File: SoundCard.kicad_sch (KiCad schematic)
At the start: 11 parts, among them J1 AudioJack3, J2 Expansion / Diag Port, J3 Conn_Coaxial, U1 SN76489AN, U2 74LS11, U3 LM386, Y1 Crystal

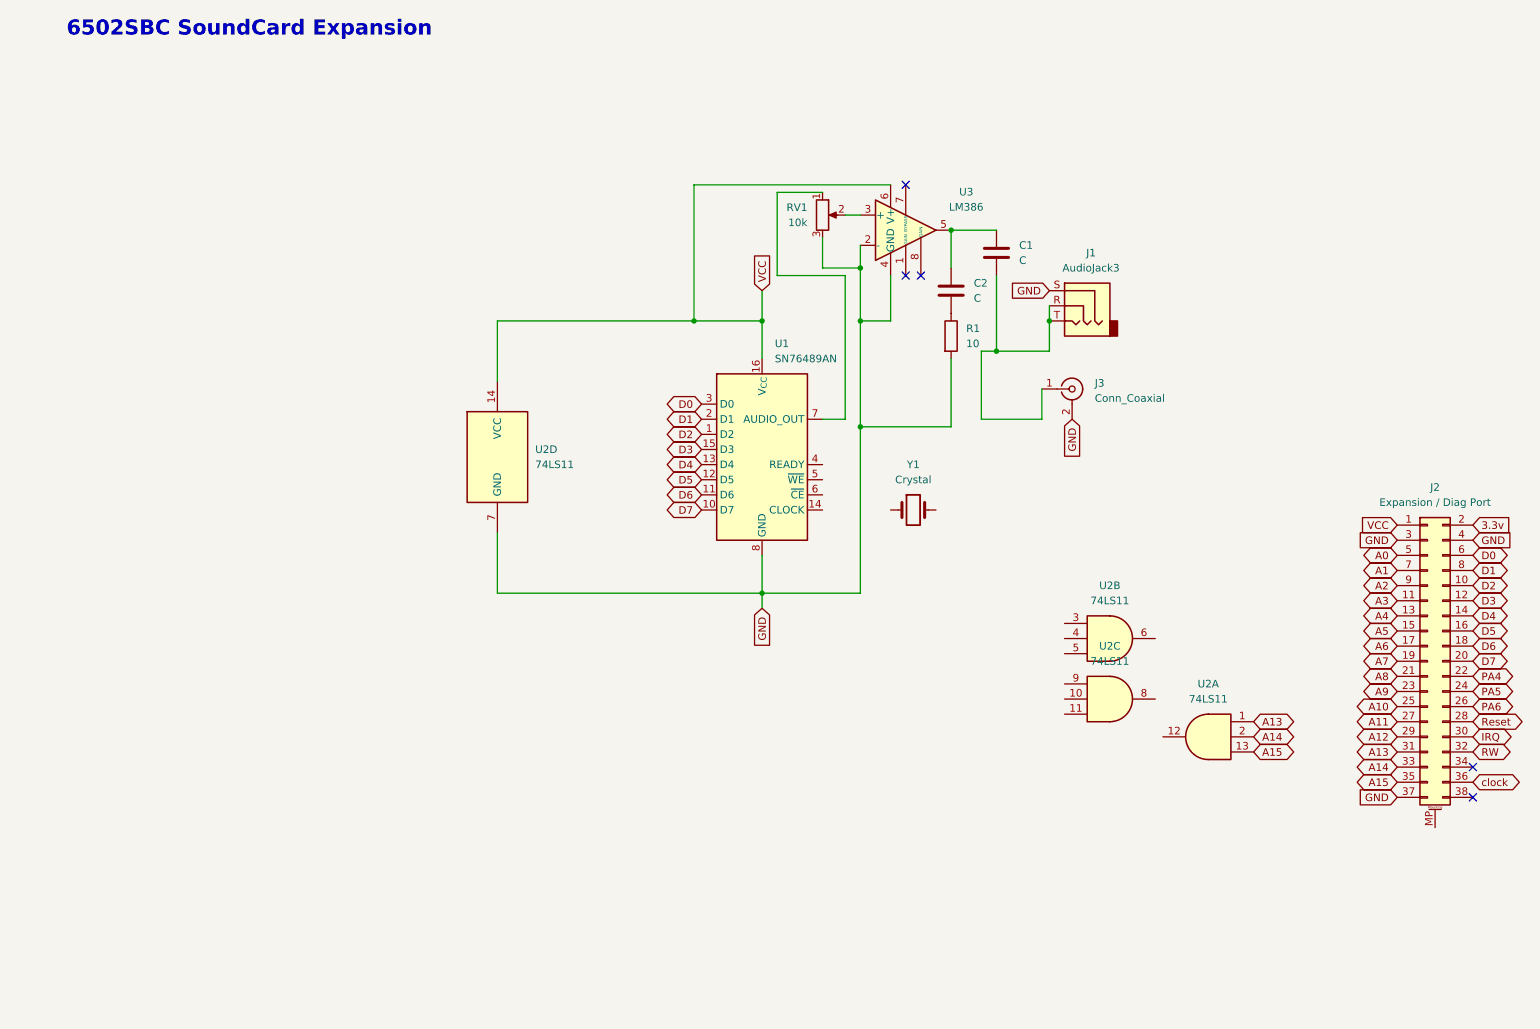
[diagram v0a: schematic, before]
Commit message: Add Sound Card
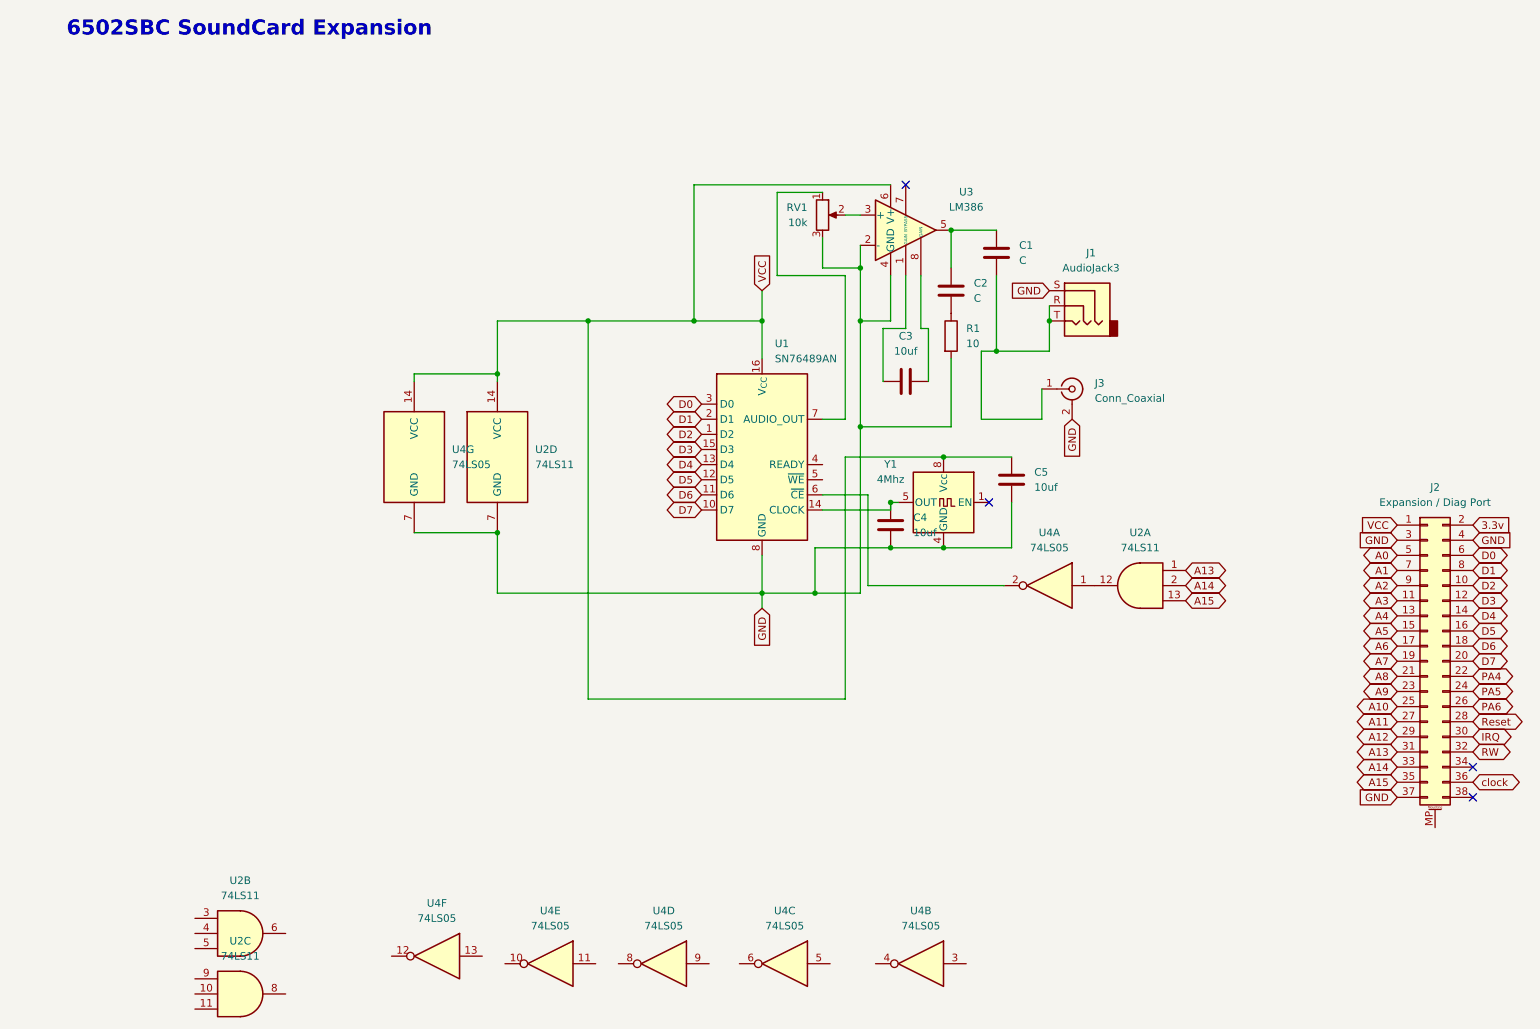
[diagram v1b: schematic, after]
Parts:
- removed Y1: Crystal, symbol Device:Crystal
- added C3, C4, C5: 10uf, symbol Device:C
- added U4: 74LS05, symbol 74xx:74LS05
- added Y1: 4Mhz, Oscillator:Oscillator_DIP-8, symbol Oscillator:CXO_DIP8
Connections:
- net GND: now also C4.1, C5.1, U4.7 (GND), Y1.4 (GND)
- net VCC: now also C5.2, U4.14 (VCC), Y1.8 (Vcc)
- net at U1.14 (CLOCK): now also C4.2, Y1.5 (OUT)
- net at U1.6 (~{CE}): now also U4.2
- net at U2.12: now also U4.1
- net at U3.1 (GAIN): now also C3.1
- net at U3.8 (GAIN): now also C3.2
- no-connect marks 5 -> 4
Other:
- moved on the sheet: U2A, U2B, U2C

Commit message: Finished Sound Card
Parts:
- added C6, C7, C8: 10uf, Capacitor_THT:C_Disc_D4.3mm_W1.9mm_P5.00mm, symbol Device:C
- C1, C2: footprint (none) -> Capacitor_THT:C_Radial_D5.0mm_H5.0mm_P2.00mm
- C3, C4, C5: footprint (none) -> Capacitor_THT:C_Disc_D4.3mm_W1.9mm_P5.00mm
- J1: footprint (none) -> Connector_Audio:Jack_3.5mm_CUI_SJ1-3513N_Horizontal
- J3: footprint (none) -> Connector_Coaxial:BNC_Amphenol_B6252HB-NPP3G-50_Horizontal
- R1: footprint (none) -> Resistor_THT:R_Axial_DIN0414_L11.9mm_D4.5mm_P7.62mm_Vertical
- RV1: footprint (none) -> Potentiometer_THT:Potentiometer_ACP_CA9-V10_Vertical_Hole
- U2, U4: footprint (none) -> Package_DIP:DIP-14_W7.62mm
- U3: footprint (none) -> Package_DIP:DIP-8_W7.62mm
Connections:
- net A0: now also U4.5
- net A1: now also U1.4 (READY)
- net A14: now also U4.3; no longer U2.2
- net GND: now also C6.1, C7.1, C8.1
- net VCC: now also C6.2, C7.2, C8.2
- net at U4.4: now also U2.2
- net at U1.5 (~{WE}): now also U4.6
- no-connect marks 4 -> 19
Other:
- note added: "Assigned to address 0xA000"
- note added: "Ready is 0xA002 and WE is 0xA001"
- moved on the sheet: U4B, U4C

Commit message: bom and sound app
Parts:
- R1: footprint Resistor_THT:R_Axial_DIN0414_L11.9mm_D4.5mm_P7.62mm_Vertical -> Resistor_THT:R_Axial_DIN0204_L3.6mm_D1.6mm_P5.08mm_Horizontal
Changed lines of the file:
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@@
 			)
 		)
-		(property "Footprint" "Resistor_THT:R_Axial_DIN0414_L11.9mm_D4.5mm_P7.62mm_Vertical"
+		(property "Footprint" "Resistor_THT:R_Axial_DIN0204_L3.6mm_D1.6mm_P5.08mm_Horizontal"
 			(at 169.672 71.12 90)
 			(effects

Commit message: x4
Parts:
- C1, C2: value C -> 10uf; footprint Capacitor_THT:C_Radial_D5.0mm_H5.0mm_P2.00mm -> Resistor_THT:R_Axial_DIN0204_L3.6mm_D1.6mm_P5.08mm_Horizontal
- RV1: footprint Potentiometer_THT:Potentiometer_ACP_CA9-V10_Vertical_Hole -> Potentiometer_THT:Potentiometer_Bourns_3296W_Vertical
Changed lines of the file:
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@@
 			)
 		)
-		(property "Value" "C"
+		(property "Value" "10uf"
 			(at 175.26 64.7699 0)
 			(effects
@@
 			)
 		)
-		(property "Footprint" "Capacitor_THT:C_Radial_D5.0mm_H5.0mm_P2.00mm"
+		(property "Footprint" "Resistor_THT:R_Axial_DIN0204_L3.6mm_D1.6mm_P5.08mm_Horizontal"
 			(at 172.4152 67.31 0)
 			(effects
@@
 			)
 		)
-		(property "Value" "C"
+		(property "Value" "10uf"
 			(at 182.88 58.4199 0)
 			(effects
@@
 			)
 		)
-		(property "Footprint" "Capacitor_THT:C_Radial_D5.0mm_H5.0mm_P2.00mm"
+		(property "Footprint" "Resistor_THT:R_Axial_DIN0204_L3.6mm_D1.6mm_P5.08mm_Horizontal"
 			(at 180.0352 60.96 0)
 			(effects
@@
 			)
 		)
-		(property "Footprint" "Potentiometer_THT:Potentiometer_ACP_CA9-V10_Vertical_Hole"
+		(property "Footprint" "Potentiometer_THT:Potentiometer_Bourns_3296W_Vertical"
 			(at 149.86 50.8 0)
 			(effects
